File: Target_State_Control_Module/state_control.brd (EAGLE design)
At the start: 68.2 x 41.9 mm, 29 parts, among them Q9 8MHz, U1 ATMEGA328P_PDIP, U2 FT232RLSSOP, X2 USBSMD

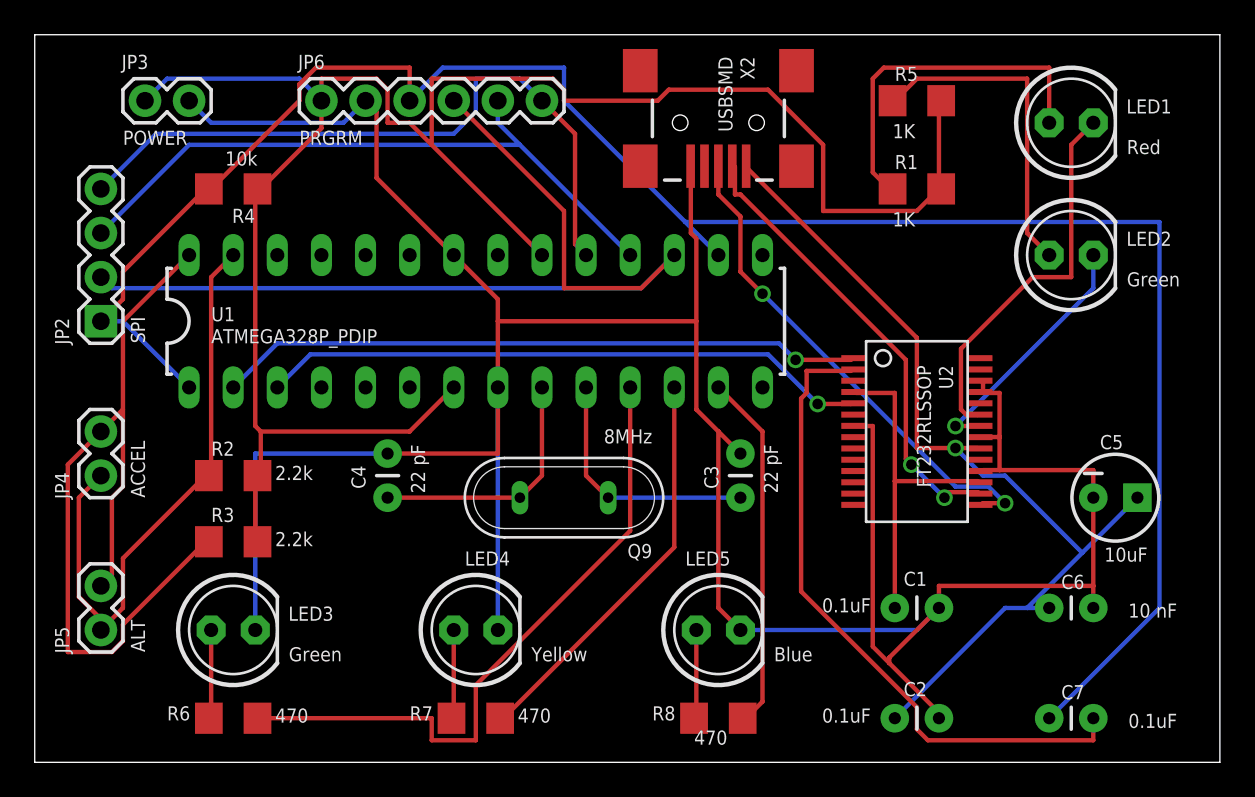
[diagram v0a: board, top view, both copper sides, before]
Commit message: added GPIO
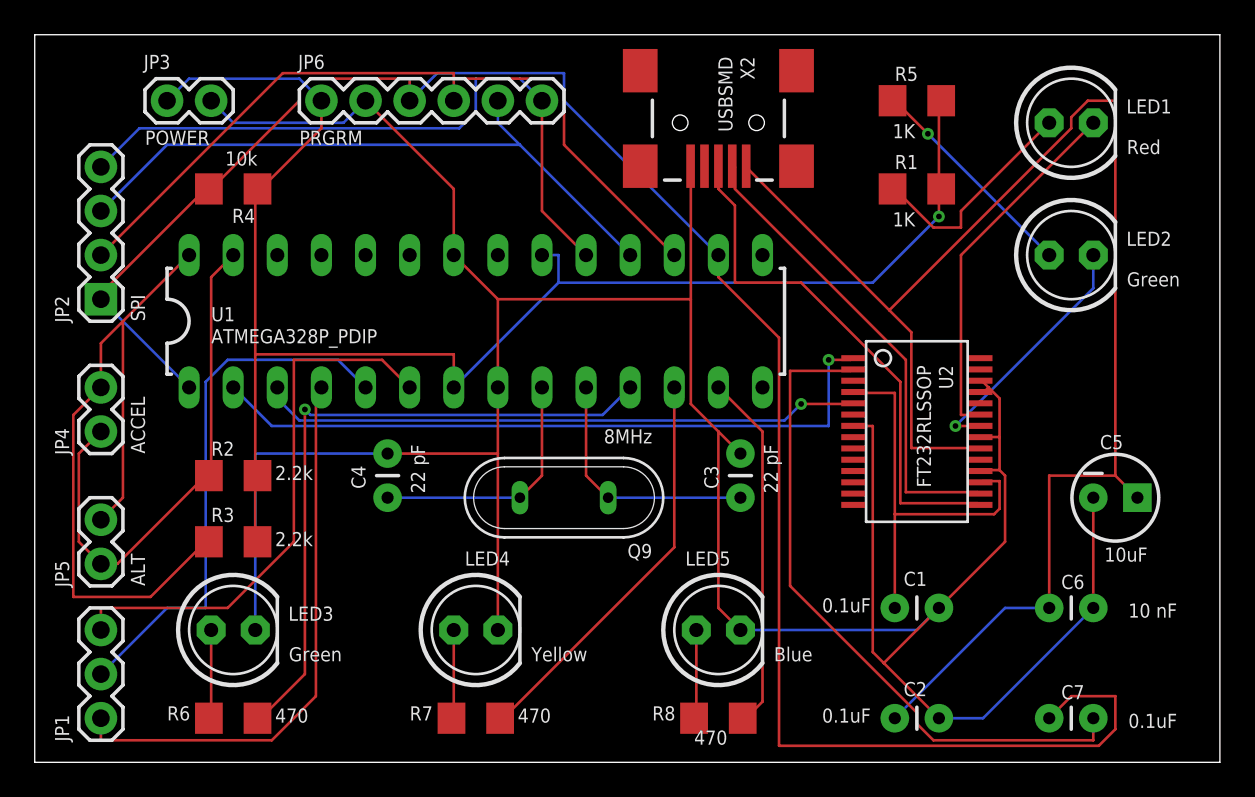
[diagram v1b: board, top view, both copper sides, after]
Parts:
- added JP1: GPIO, SparkFun-Connectors:1X03
- moved JP5 3.81 mm to (3.81, 49.5)
- moved JP4 2.54 mm to (3.81, 57.1)
- moved JP3 1.27 mm to (7.62, 76.2)
- moved JP2 1.27 mm to (3.81, 64.8)
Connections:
- new net INT0: JP1.1, U1.4
- new net INT1: JP1.2, U1.5
- new net IO4: JP1.3, U1.6
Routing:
- net VBUS: track 54.3 -> 88.9 mm, vias 1 -> 0
- net INT0: track 0.00 -> 32.6 mm
- net IO4: track 0.00 -> 31.8 mm
- net INT1: track 0.00 -> 31.0 mm
- net 3.3V: track 115.6 -> 92.2 mm, vias 0 -> 1
- net MOSI: track 54.6 -> 45.0 mm
- net N$1: track 20.5 -> 13.0 mm
- net N$2: track 19.0 -> 12.7 mm, vias 0 -> 1
- net SS: track 116.5 -> 111.5 mm
- net SDA: track 34.7 -> 30.4 mm
- net SCL: track 47.8 -> 43.5 mm
- net N$4: track 19.7 -> 23.6 mm
- net TXO: track 37.2 -> 40.5 mm
- net USB_D+: track 28.8 -> 30.6 mm, vias 2 -> 0
- net GND-ISO: track 181.8 -> 180.5 mm
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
